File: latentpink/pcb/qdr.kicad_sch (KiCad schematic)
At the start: 57 parts, among them U2 XC7K160T-2FBG484C, U3 CY7C2245KV18-450BZXI

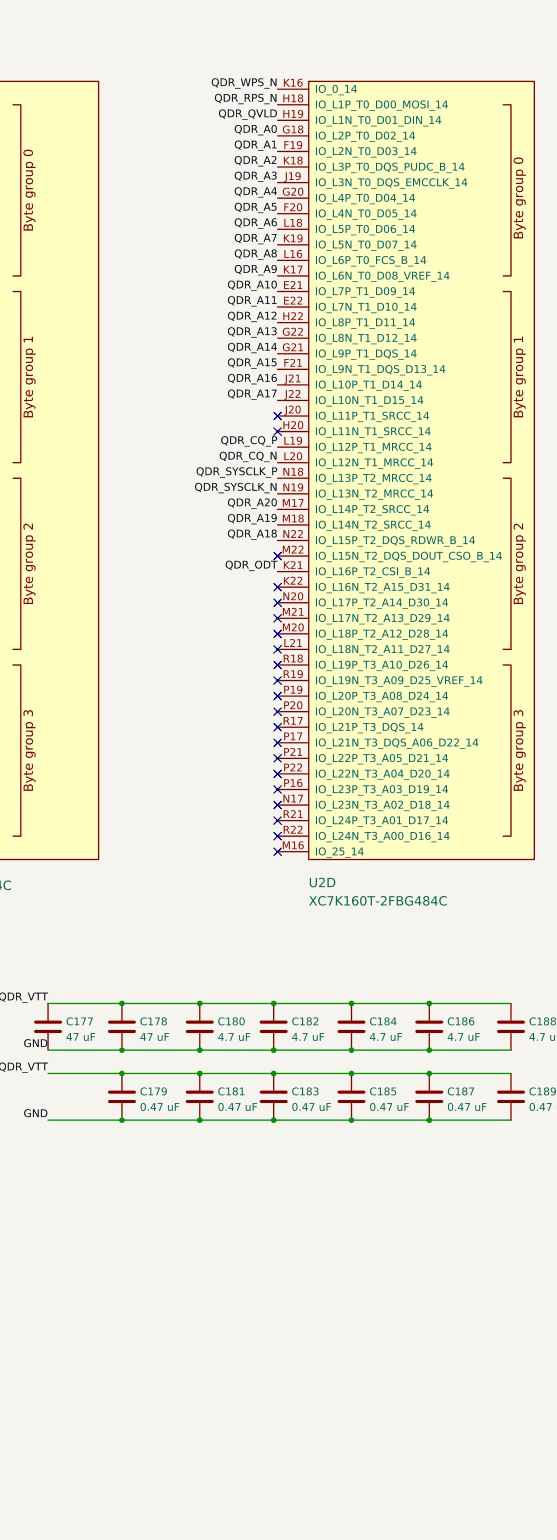
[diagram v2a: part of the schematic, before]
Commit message: Initial version of RGMII PHY schematic
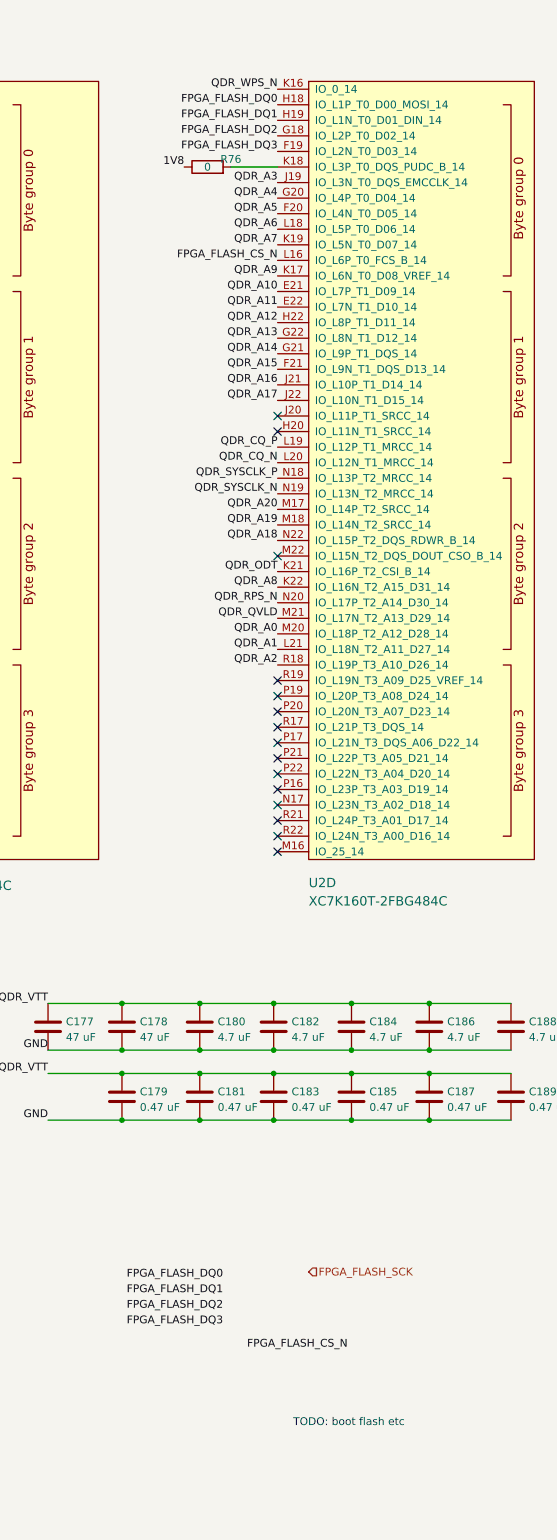
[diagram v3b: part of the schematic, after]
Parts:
- added R76: 0, symbol device:R
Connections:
- net 1V8: now also R76.1
- net QDR_A0: now also U2.M20 (IO_L18P_T2_A12_D28_14); no longer U2.G18 (IO_L2P_T0_D02_14)
- net QDR_A1: now also U2.L21 (IO_L18N_T2_A11_D27_14); no longer U2.F19 (IO_L2N_T0_D03_14)
- net QDR_A2: now also U2.R18 (IO_L19P_T3_A10_D26_14); no longer U2.K18 (IO_L3P_T0_DQS_PUDC_B_14)
- net QDR_A8: now also U2.K22 (IO_L16N_T2_A15_D31_14); no longer U2.L16 (IO_L6P_T0_FCS_B_14)
- net QDR_QVLD: now also U2.M21 (IO_L17N_T2_A13_D29_14); no longer U2.H19 (IO_L1N_T0_D01_DIN_14)
- net QDR_RPS_N: now also U2.N20 (IO_L17P_T2_A14_D30_14); no longer U2.H18 (IO_L1P_T0_D00_MOSI_14)
- new net: R76.2, U2.K18 (IO_L3P_T0_DQS_PUDC_B_14)
- new net FPGA_FLASH_CS_N: U2.L16 (IO_L6P_T0_FCS_B_14)
- new net FPGA_FLASH_DQ0: U2.H18 (IO_L1P_T0_D00_MOSI_14)
- new net FPGA_FLASH_DQ1: U2.H19 (IO_L1N_T0_D01_DIN_14)
- new net FPGA_FLASH_DQ2: U2.G18 (IO_L2P_T0_D02_14)
- new net FPGA_FLASH_DQ3: U2.F19 (IO_L2N_T0_D03_14)
- no-connect marks 45 -> 39
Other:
- note added: "TODO: boot flash etc"
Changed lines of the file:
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@@
   (paper "A3")
   (title_block
-    (date "2023-05-07")
+    (date "2023-05-10")
     (rev "0.1")
     (company "Antikernel Labs")
@@
   (no_connect (at 269.24 142.24))
   (no_connect (at 269.24 144.78))
-  (no_connect (at 269.24 111.76))
   (no_connect (at 269.24 132.08))
   (no_connect (at 198.12 25.4))
@@
   (no_connect (at 269.24 149.86))
   (no_connect (at 198.12 132.08))
-  (no_connect (at 269.24 109.22))
   (no_connect (at 346.71 101.6))
   (no_connect (at 269.24 101.6))
-  (no_connect (at 269.24 116.84))
   (no_connect (at 269.24 134.62))
   (no_connect (at 269.24 121.92))
@@
   (no_connect (at 33.02 176.53))
   (no_connect (at 346.71 149.86))
-  (no_connect (at 269.24 119.38))
   (no_connect (at 269.24 137.16))
   (no_connect (at 269.24 147.32))
@@
   (no_connect (at 198.12 149.86))
   (no_connect (at 346.71 86.36))
-  (no_connect (at 269.24 114.3))
-  (no_connect (at 269.24 106.68))
   (no_connect (at 200.66 266.7))
   (wire (pts (xy 88.9 209.55) (xy 101.6 209.55))
@@
     (stroke (width 0) (type default) (color 0 0 0 0))
   )
+  (wire (pts (xy 261.62 38.1) (xy 269.24 38.1))
+    (stroke (width 0) (type default) (color 0 0 0 0))
+  )
   (wire (pts (xy 33.02 212.09) (xy 33.02 214.63))
     (stroke (width 0) (type default) (color 0 0 0 0))
@@
     (effects (font (size 1.27 1.27)) (justify left bottom))
   )
+  (text "TODO: boot flash etc" (at 271.78 243.84 0)
+    (effects (font (size 1.27 1.27)) (justify left bottom))
+  )
   (label "QDR_D28" (at 31.75 113.03 180)
     (effects (font (size 1.27 1.27)) (justify right bottom))
@@
     (effects (font (size 1.27 1.27)) (justify right bottom))
   )
+  (label "FPGA_FLASH_DQ0" (at 260.35 219.71 180)
+    (effects (font (size 1.27 1.27)) (justify right bottom))
+  )
   (label "QDR_Q22" (at 346.71 104.14 180)
     (effects (font (size 1.27 1.27)) (justify right bottom))
@@
     (effects (font (size 1.27 1.27)) (justify right bottom))
   )
+  (label "FPGA_FLASH_DQ0" (at 269.24 27.94 180)
+    (effects (font (size 1.27 1.27)) (justify right bottom))
+  )
   (label "GND" (at 231.775 182.245 180)
     (effects (font (size 1.27 1.27)) (justify right bottom))
@@
     (effects (font (size 1.27 1.27)) (justify right bottom))
   )
+  (label "FPGA_FLASH_CS_N" (at 280.67 231.14 180)
+    (effects (font (size 1.27 1.27)) (justify right bottom))
+  )
   (label "QDR_A9" (at 132.08 110.49 180)
     (effects (font (size 1.27 1.27)) (justify right bottom))
@@
     (effects (font (size 1.27 1.27)) (justify right bottom))
   )
-  (label "QDR_A0" (at 269.24 33.02 180)
+  (label "QDR_A0" (at 269.24 114.3 180)
     (effects (font (size 1.27 1.27)) (justify right bottom))
   )
@@
     (effects (font (size 1.27 1.27)) (justify right bottom))
   )
+  (label "FPGA_FLASH_CS_N" (at 269.24 53.34 180)
+    (effects (font (size 1.27 1.27)) (justify right bottom))
+  )
   (label "QDR_A20" (at 200.66 176.53 180)
     (effects (font (size 1.27 1.27)) (justify right bottom))
   )
+  (label "1V8" (at 254 38.1 180)
+    (effects (font (size 1.27 1.27)) (justify right bottom))
+  )
   (label "QDR_Q12" (at 346.71 66.04 180)
     (effects (font (size 1.27 1.27)) (justify right bottom))
@@
     (effects (font (size 1.27 1.27)) (justify right bottom))
   )
+  (label "FPGA_FLASH_DQ2" (at 269.24 33.02 180)
+    (effects (font (size 1.27 1.27)) (justify right bottom))
+  )
   (label "QDR_A18" (at 132.08 29.21 180)
     (effects (font (size 1.27 1.27)) (justify right bottom))
@@
     (effects (font (size 1.27 1.27)) (justify right bottom))
   )
-  (label "QDR_A1" (at 269.24 35.56 180)
+  (label "QDR_A1" (at 269.24 116.84 180)
     (effects (font (size 1.27 1.27)) (justify right bottom))
   )
@@
     (effects (font (size 1.27 1.27)) (justify right bottom))
   )
-  (label "QDR_A8" (at 269.24 53.34 180)
+  (label "QDR_A8" (at 269.24 106.68 180)
     (effects (font (size 1.27 1.27)) (justify right bottom))
   )
@@
     (effects (font (size 1.27 1.27)) (justify right bottom))
   )
+  (label "FPGA_FLASH_DQ1" (at 269.24 30.48 180)
+    (effects (font (size 1.27 1.27)) (justify right bottom))
+  )
   (label "QDR_A14" (at 269.24 68.58 180)
     (effects (font (size 1.27 1.27)) (justify right bottom))
@@
     (effects (font (size 1.27 1.27)) (justify right bottom))
   )
+  (label "FPGA_FLASH_DQ3" (at 269.24 35.56 180)
+    (effects (font (size 1.27 1.27)) (justify right bottom))
+  )
   (label "QDR_D23" (at 198.12 106.68 180)
     (effects (font (size 1.27 1.27)) (justify right bottom))
@@
     (effects (font (size 1.27 1.27)) (justify right bottom))
   )
+  (label "FPGA_FLASH_DQ3" (at 260.35 227.33 180)
+    (effects (font (size 1.27 1.27)) (justify right bottom))
+  )
   (label "GND" (at 88.9 217.17 180)
     (effects (font (size 1.27 1.27)) (justify right bottom))
@@
     (effects (font (size 1.27 1.27)) (justify right bottom))
   )
-  (label "QDR_RPS_N" (at 269.24 27.94 180)
+  (label "QDR_RPS_N" (at 269.24 109.22 180)
     (effects (font (size 1.27 1.27)) (justify right bottom))
   )
@@
     (effects (font (size 1.27 1.27)) (justify right bottom))
   )
-  (label "QDR_A2" (at 269.24 38.1 180)
+  (label "QDR_A2" (at 269.24 119.38 180)
     (effects (font (size 1.27 1.27)) (justify right bottom))
   )
@@
     (effects (font (size 1.27 1.27)) (justify right bottom))
   )
+  (label "FPGA_FLASH_DQ2" (at 260.35 224.79 180)
+    (effects (font (size 1.27 1.27)) (justify right bottom))
+  )
   (label "QDR_D33" (at 31.75 125.73 180)
     (effects (font (size 1.27 1.27)) (justify right bottom))
@@
     (effects (font (size 1.27 1.27)) (justify right bottom))
   )
-  (label "QDR_QVLD" (at 269.24 30.48 180)
+  (label "QDR_QVLD" (at 269.24 111.76 180)
     (effects (font (size 1.27 1.27)) (justify right bottom))
   )
@@
     (effects (font (size 1.27 1.27)) (justify right bottom))
   )
+  (label "FPGA_FLASH_DQ1" (at 260.35 222.25 180)
+    (effects (font (size 1.27 1.27)) (justify right bottom))
+  )
   (label "QDR_Q32" (at 81.28 123.19 180)
     (effects (font (size 1.27 1.27)) (justify right bottom))
@@
     (effects (font (size 1.27 1.27)) (justify right))
   )
+  (hierarchical_label "FPGA_FLASH_SCK" (shape input) (at 274.32 218.44 0)
+    (effects (font (size 1.27 1.27)) (justify left))
+  )
   (hierarchical_label "QDR_VTT" (shape input) (at 210.82 173.99 0)
     (effects (font (size 1.27 1.27)) (justify left))
@@
     (pin "8")
   )
+  (symbol (lib_id "device:R") (at 257.81 38.1 90) (unit 1)
+    (in_bom yes) (on_board yes)
+    (property "Reference" "R76" (id 0) (at 261.62 36.83 90))
+    (property "Value" "0" (id 1) (at 257.81 38.1 90))
+    (property "Footprint" "" (id 2) (at 257.81 39.878 90)
+      (effects (font (size 1.27 1.27)) hide)
+    )
+    (property "Datasheet" "" (id 3) (at 257.81 38.1 0)
+      (effects (font (size 1.27 1.27)) hide)
+    )
+    (pin "1")
+    (pin "2")
+  )
   (symbol (lib_id "device:C") (at 294.005 189.865 0) (unit 1)

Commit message: Continued work on QSGMII subsystem
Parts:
- R76: footprint (none) -> azonenberg_pcb:EIA_0402_RES_NOSILK
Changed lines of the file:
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@@
   (paper "A3")
   (title_block
-    (date "2023-05-10")
+    (date "2023-05-14")
     (rev "0.1")
     (company "Antikernel Labs")
@@
     (property "Reference" "R76" (id 0) (at 261.62 36.83 90))
     (property "Value" "0" (id 1) (at 257.81 38.1 90))
-    (property "Footprint" "" (id 2) (at 257.81 39.878 90)
+    (property "Footprint" "azonenberg_pcb:EIA_0402_RES_NOSILK" (id 2) (at 257.81 39.878 90)
       (effects (font (size 1.27 1.27)) hide)
     )

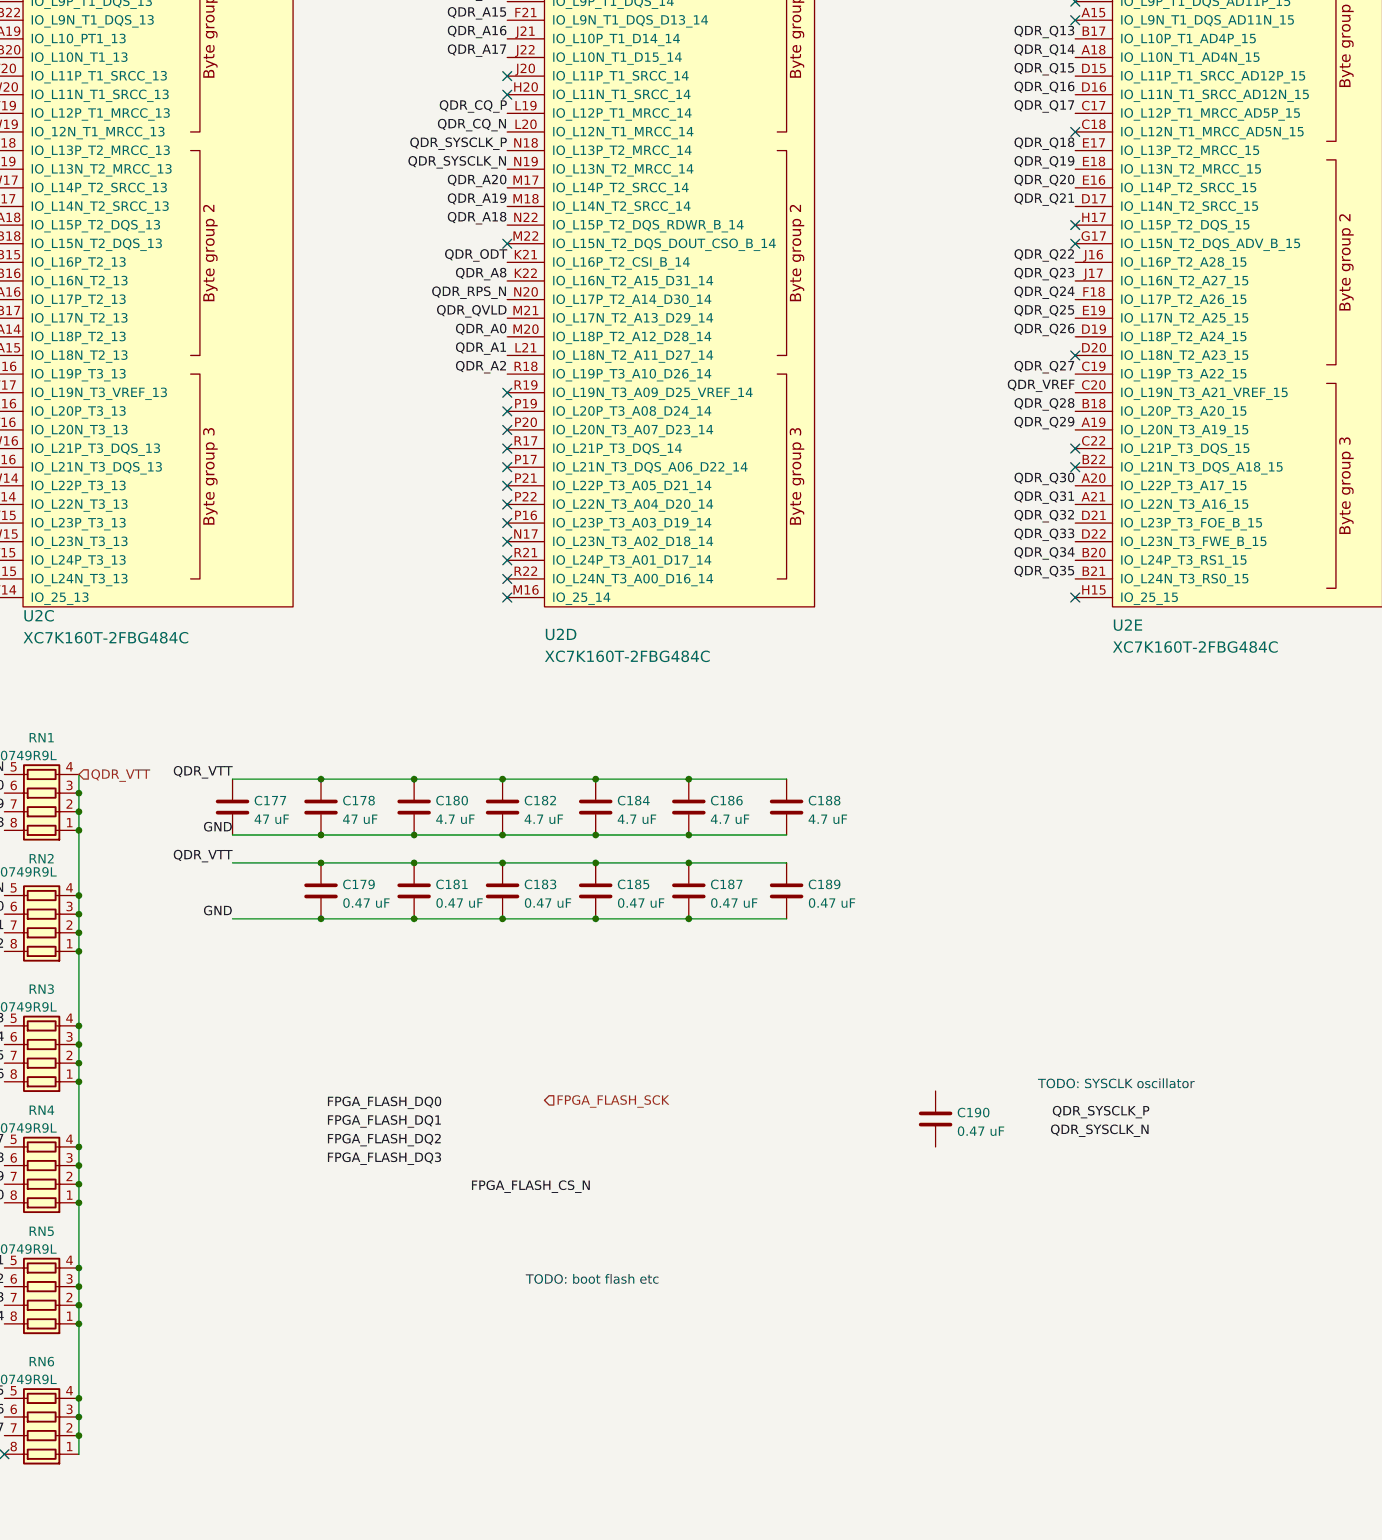
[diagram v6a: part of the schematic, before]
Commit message: Continued footprint assignment and miscellaneous missing tidbits of schematic
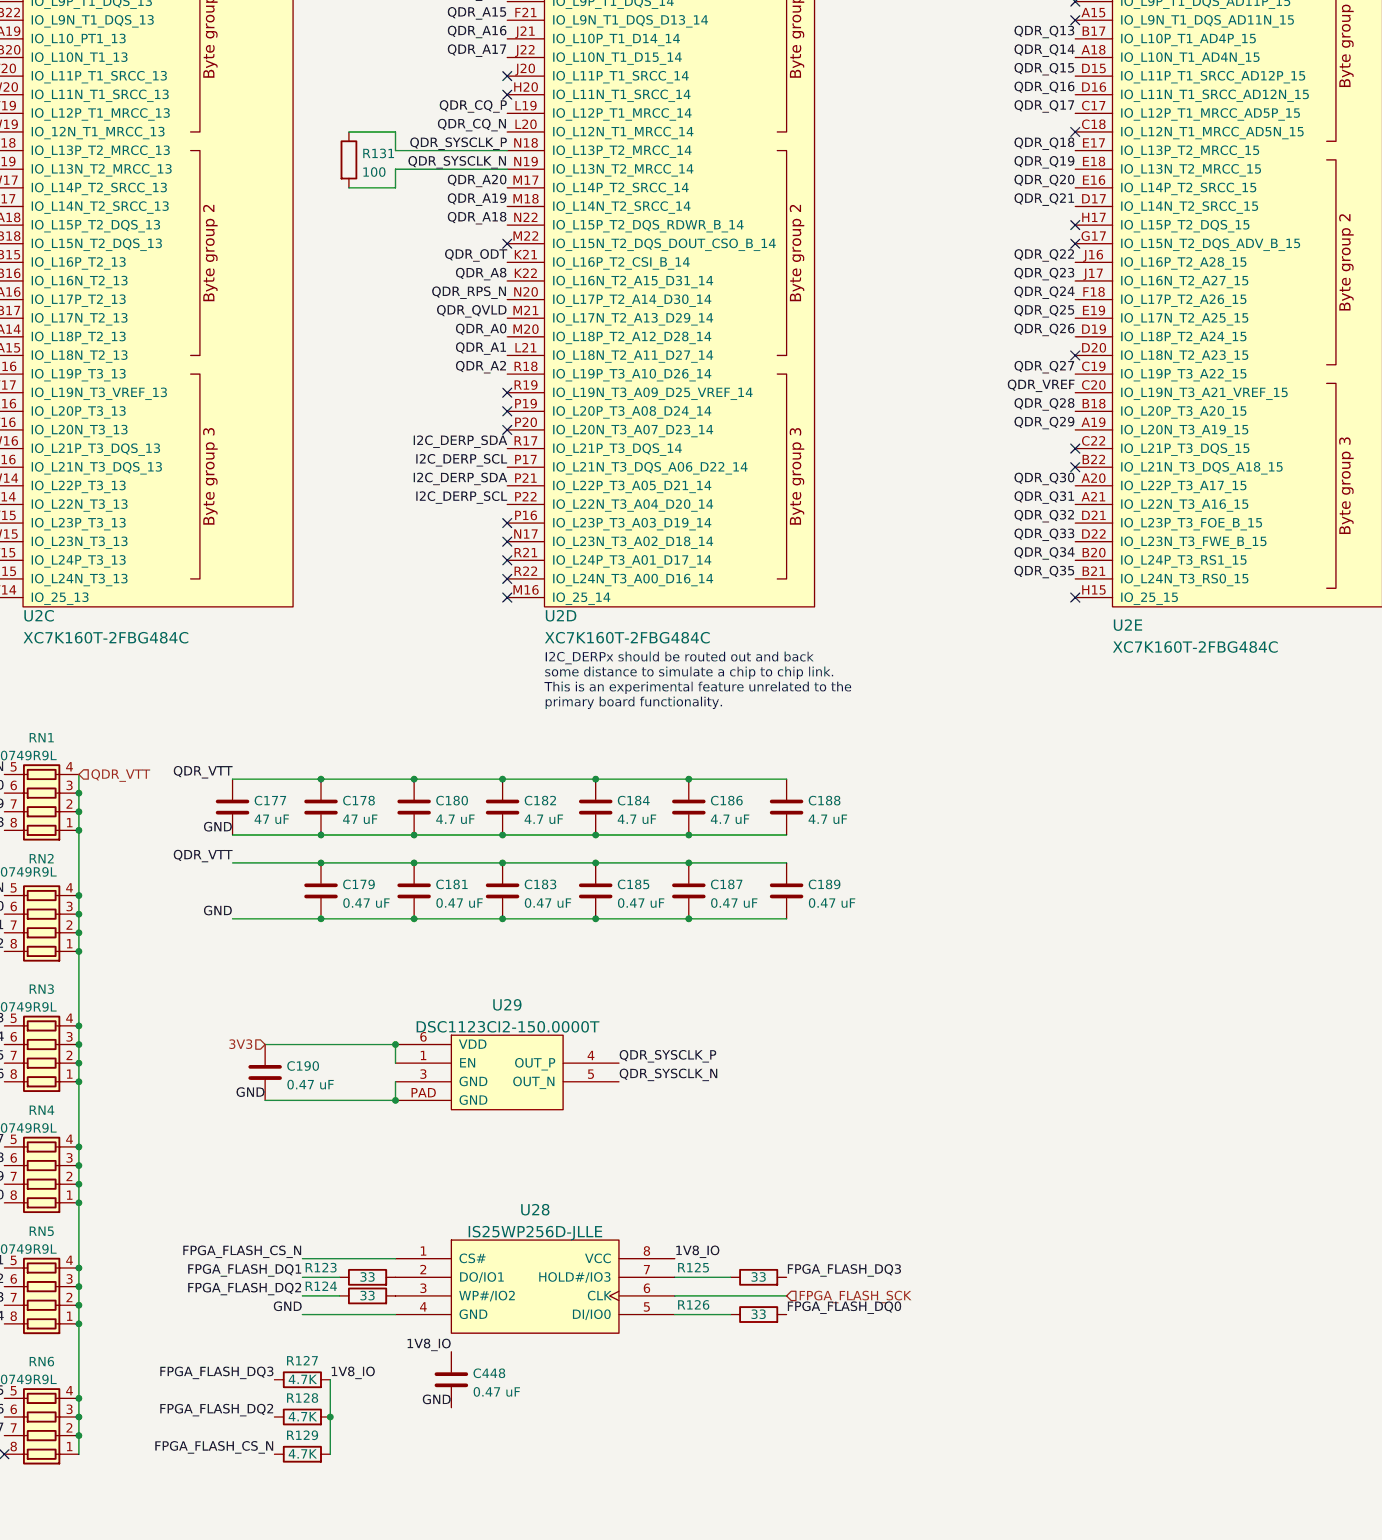
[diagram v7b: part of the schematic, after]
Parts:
- added C448: 0.47 uF, azonenberg_pcb:EIA_0402_CAP_NOSILK, symbol device:C
- added R123, R124, R125, R126: 33, azonenberg_pcb:EIA_0402_RES_NOSILK, symbol device:R
- added R127, R128, R129: 4.7K, azonenberg_pcb:EIA_0402_RES_NOSILK, symbol device:R
- added R131: 100, azonenberg_pcb:EIA_0402_RES_NOSILK, symbol device:R
- added U28: IS25WP256D-JLLE, azonenberg_pcb:DFN_8_1.27MM_8x6MM, symbol memory-azonenberg:W25Q80BV
- added U29: DSC1123CI2-150.0000T, azonenberg_pcb:OSCILLATOR_LVDS_3.2x2.5, symbol osc-azonenberg:OSC_LVDS
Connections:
- net 1V8_IO: now also C448.1, R127.2, R128.2, R129.2, U28.8 (VCC)
- net FPGA_FLASH_CS_N: now also R129.1, U28.1 (CS#)
- net FPGA_FLASH_DQ0: now also R126.2
- net FPGA_FLASH_DQ1: now also R123.1
- net FPGA_FLASH_DQ2: now also R124.1, R128.1
- net FPGA_FLASH_DQ3: now also R125.2, R127.1
- net FPGA_FLASH_SCK: now also U28.6 (CLK)
- net GND: now also C190.2, C448.2, U28.4 (GND), U29.3 (GND), U29.PAD (GND)
- net QDR_SYSCLK_N: now also R131.2, U29.5 (OUT_N)
- net QDR_SYSCLK_P: now also R131.1, U29.4 (OUT_P)
- net I2C_DERP_SCL: now reaches U2.P17 (IO_L21N_T3_DQS_A06_D22_14)
- net I2C_DERP_SCL: now also U2.P22 (IO_L22N_T3_A04_D20_14)
- net I2C_DERP_SDA: now reaches U2.P21 (IO_L22P_T3_A05_D21_14)
- net I2C_DERP_SDA: now also U2.R17 (IO_L21P_T3_DQS_14)
- net 3V3: now reaches C190.1
- net 3V3: now also U29.1 (EN), U29.6 (VDD)
- new net: R124.2, U28.3 (WP#/IO2)
- new net: R123.2, U28.2 (DO/IO1)
- new net: R125.1, U28.7 (HOLD#/IO3)
- new net: R126.1, U28.5 (DI/IO0)
- no-connect marks 39 -> 35
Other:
- note added: "I2C_DERPx should be routed out and back some distance to simulate a chip to chip link. This is an experimental feature unrelated to the primary board functionality."
- note removed: "TODO: SYSCLK oscillator"
- note removed: "TODO: boot flash etc"
- moved on the sheet: C190
